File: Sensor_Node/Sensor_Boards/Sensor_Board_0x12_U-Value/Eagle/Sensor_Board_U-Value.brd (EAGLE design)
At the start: 31.5 x 57 mm, 25 parts, among them IC1 MCP3911A0-E/SS, IC2 4066D, J2 ARDUINO_ISP, U2 ATMEGA328P_TQFP, Y1 8MHZ

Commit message: Added WSN eagle library
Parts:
- moved D2 103.3 mm to (52.0, 22.0), turned to 180 degrees
- moved R1 101.1 mm to (52.0, 24.0), turned to 180 degrees
- moved Y1 94.3 mm to (50.4, 7.74)
- moved R4 84.0 mm to (47.5, 24.0)
- moved C12 83.7 mm to (43.0, 7.50)
- moved R3 78.1 mm to (47.5, 22.0), turned to 180 degrees
- moved S3 77.5 mm to (37.0, 25.5), turned to 90 degrees
- moved J2 74.6 mm to (50.0, 28.3), turned to 90 degrees
- moved C6 74.1 mm to (46.5, 7.50), turned to 180 degrees
- moved S2 57.7 mm to (38.0, 14.0), turned to 270 degrees
- moved U2 56.8 mm to (47.9, 14.6), turned to 90 degrees
- moved J1 34.2 mm to (2.34, 22.5), turned to 180 degrees
- moved D1 33.1 mm to (7.00, 17.0), turned to 0 degrees
- moved C8 29.7 mm to (7.00, 22.0), turned to 90 degrees
- moved C3 27.4 mm to (17.5, 8.50)
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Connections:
- removed net D11_MOSI: U2.15
- removed net D12_MISO: J2.P$1, J2.P$3, U2.16
- removed net D13_SCK: J2.P$2, U2.17
- removed net N$16: U2.32
- removed net N$20: U2.10
- removed net N$21: U2.11
- net ADCLK: now also U2.32
- net AD_CS: now also U2.10
- net DATA_READY: now also U2.11
- net MISO: now also J2.P$1, U2.16
- net MOSI: now also J2.P$3, U2.15
- net SCK: now also J2.P$2, U2.17
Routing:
- net DVDD: track 58.3 -> 0.00 mm
- net INPUT_EN: track 50.2 -> 0.00 mm
- net SHORT: track 48.8 -> 0.00 mm, vias 2 -> 0
- net DGND: track 43.5 -> 0.00 mm, vias 3 -> 0
- net N$8: track 25.0 -> 0.00 mm, vias 2 -> 0
- net AVDD: track 19.9 -> 0.00 mm
- net ADCLK: track 14.1 -> 0.00 mm
- net DATA_READY: track 14.1 -> 0.00 mm
- net N$12: track 12.1 -> 0.00 mm
- net N$2: track 3.74 -> 0.00 mm
- net MOSI: track 2.08 -> 0.00 mm
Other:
- board size 31.5 x 57 mm -> 55 x 35 mm

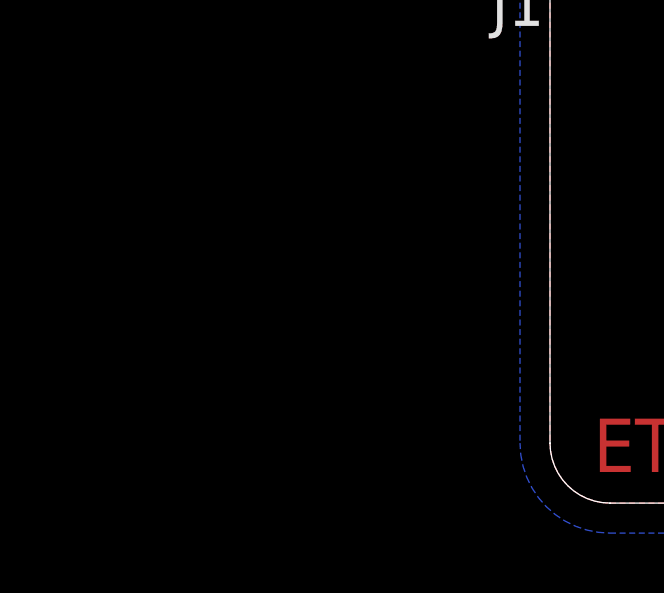
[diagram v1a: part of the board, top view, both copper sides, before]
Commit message: Update U-Value board, Added Readme for sensor boards
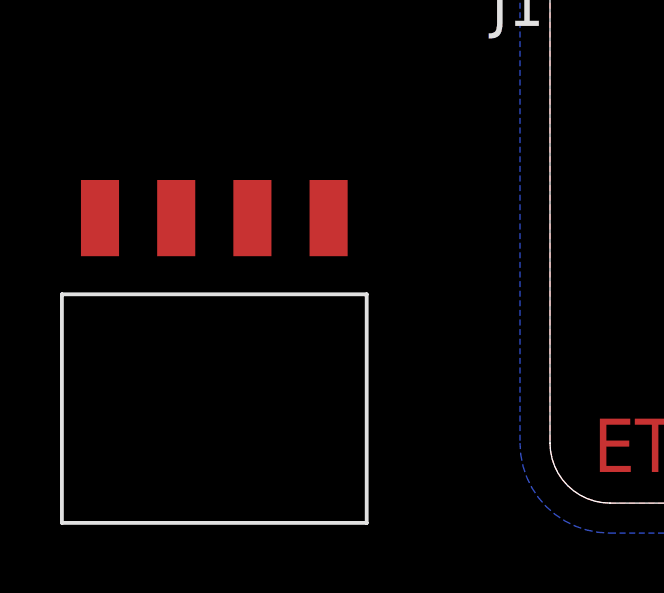
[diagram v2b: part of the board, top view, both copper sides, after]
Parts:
- added U$1: M04_SMD_90, wsn:M04_SMD_90
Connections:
- removed net N$19: U2.9
- removed net N$22: U2.12
- new net MCU_RXI: U$1.2, U2.13
- new net MCU_TXO: U$1.3, U2.12
- net GND: now also U$1.1
- net LED: now also U2.9; no longer U2.13
- net VCC: now also U$1.4
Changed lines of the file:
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@@
 </element>
 <element name="D2" library="wsn" package="LED-0603" value="" x="52" y="22" rot="R180"/>
+<element name="U$1" library="wsn" package="M04_SMD_90" value="M04_SMD_90" x="-15" y="9.5"/>
 </elements>
 <signals>
@@
 <contactref element="S2" pad="1"/>
 <contactref element="J2" pad="P$6"/>
+<contactref element="U$1" pad="4"/>
 <wire x1="49.8725" y1="18.8551" x2="48.4" y2="24" width="0" layer="19" extent="1-1"/>
 <wire x1="44.9025" y1="28.2675" x2="48.4" y2="24" width="0" layer="19" extent="1-1"/>
@@
 <wire x1="42.1" y1="7.5" x2="47.4725" y2="10.2699" width="0" layer="19" extent="1-1"/>
 <wire x1="35.3" y1="16.5" x2="42.1" y2="7.5" width="0" layer="19" extent="1-1"/>
+<wire x1="-7.38" y1="9.5" x2="35.3" y2="16.5" width="0" layer="19" extent="1-1"/>
 </signal>
 <signal name="GND">
@@
 <contactref element="Y1" pad="2"/>
 <contactref element="D2" pad="C"/>
+<contactref element="U$1" pad="1"/>
 <wire x1="37" y1="33.45" x2="44.9025" y2="30.8075" width="0" layer="19" extent="1-1"/>
 <wire x1="37" y1="25.5" x2="37" y2="33.45" width="0" layer="19" extent="1-1"/>
@@
 <wire x1="50.4" y1="7.735" x2="48.2725" y2="10.2699" width="0" layer="19" extent="1-1"/>
 <wire x1="35.3" y1="11.5" x2="43.9" y2="7.5" width="0" layer="19" extent="1-1"/>
+<wire x1="-15" y1="9.5" x2="35.3" y2="11.5" width="0" layer="19" extent="1-1"/>
 </signal>
 <signal name="N$5">
@@
 <contactref element="U2" pad="2"/>
 </signal>
-<signal name="N$19">
+<signal name="LED">
+<contactref element="R1" pad="2"/>
 <contactref element="U2" pad="9"/>
-</signal>
-<signal name="N$22">
-<contactref element="U2" pad="12"/>
-</signal>
-<signal name="LED">
-<contactref element="U2" pad="13"/>
-<contactref element="R1" pad="2"/>
-<wire x1="52.1651" y1="14.9625" x2="51.1" y2="24" width="0" layer="19" extent="1-1"/>
+<wire x1="52.1651" y1="11.7625" x2="51.1" y2="24" width="0" layer="19" extent="1-1"/>
 </signal>
 <signal name="D10_SS">
@@
 <contactref element="S2" pad="4"/>
 </signal>
+<signal name="MCU_TXO">
+<contactref element="U$1" pad="3"/>
+<contactref element="U2" pad="12"/>
+<wire x1="-9.92" y1="9.5" x2="52.1651" y2="14.1625" width="0" layer="19" extent="1-1"/>
+</signal>
+<signal name="MCU_RXI">
+<contactref element="U$1" pad="2"/>
+<contactref element="U2" pad="13"/>
+<wire x1="-12.46" y1="9.5" x2="52.1651" y2="14.9625" width="0" layer="19" extent="1-1"/>
+</signal>
 </signals>

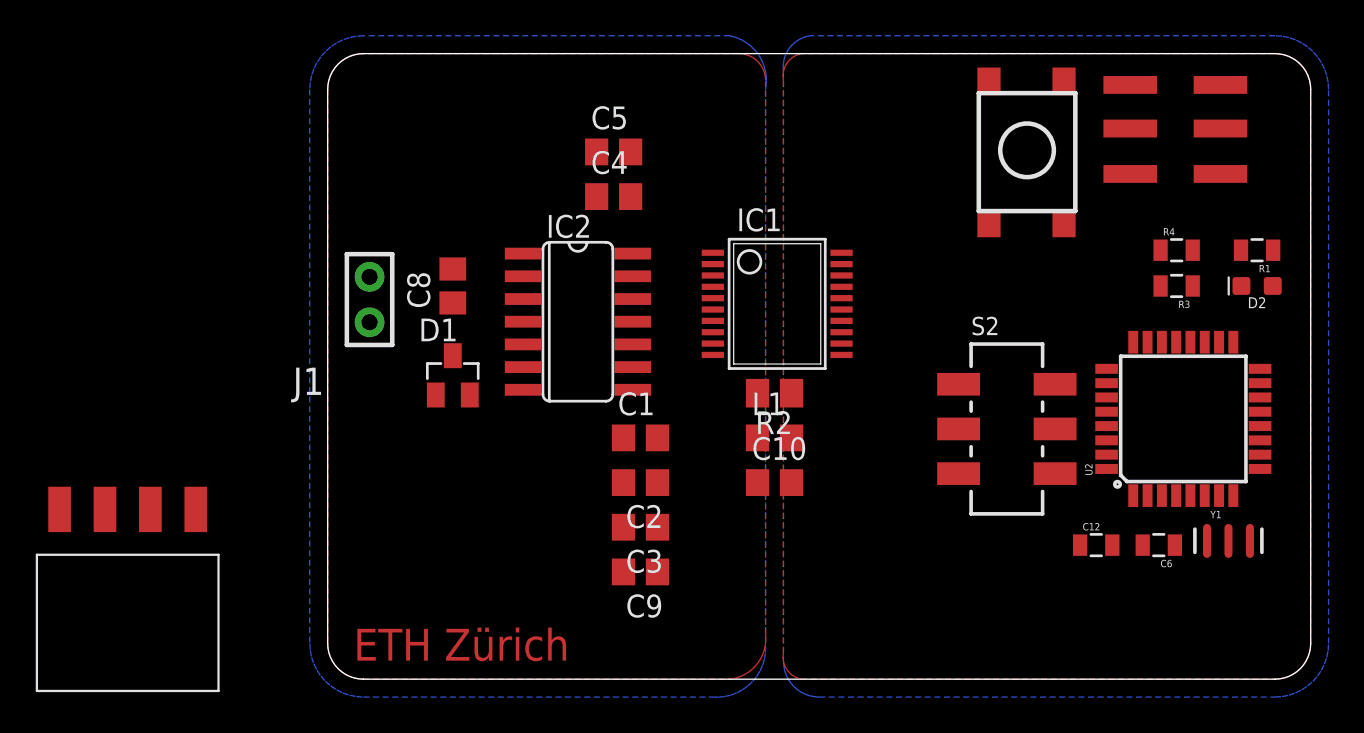
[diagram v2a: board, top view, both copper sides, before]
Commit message: Updated gatway board, updated u-value board
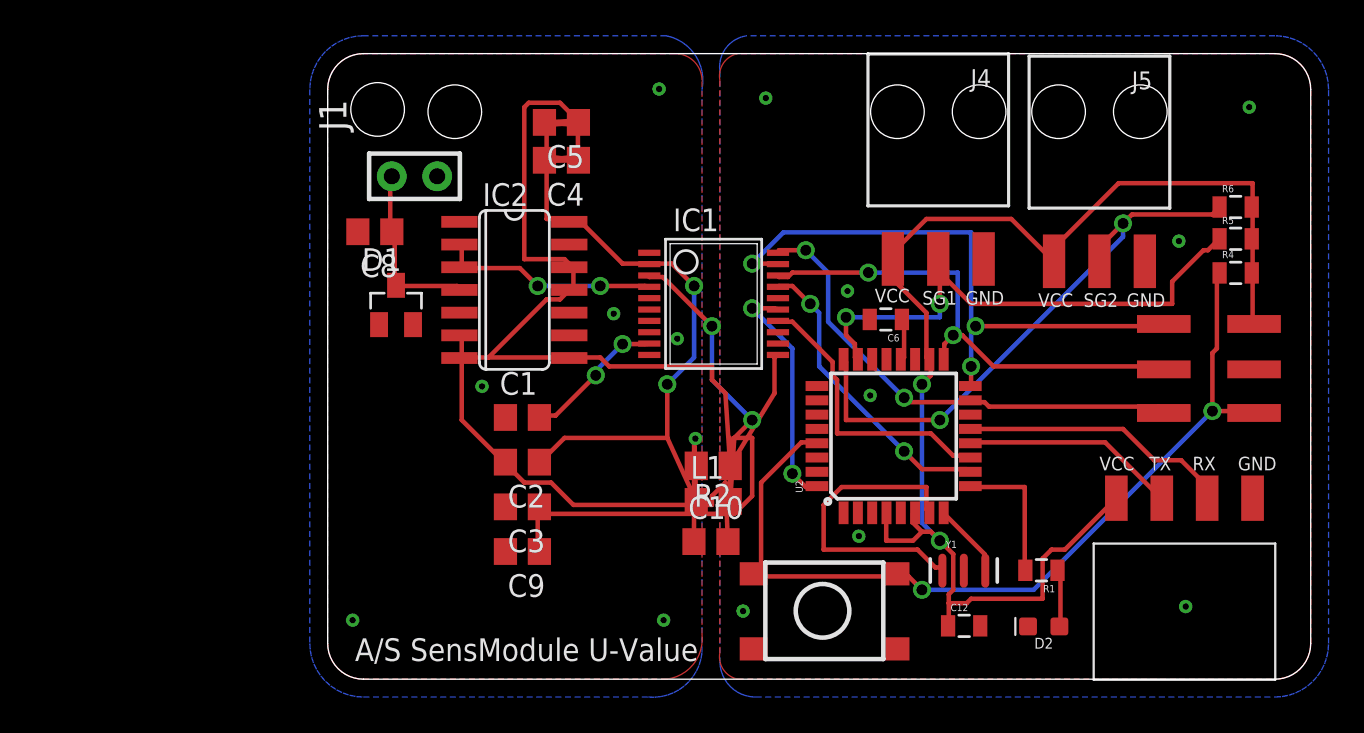
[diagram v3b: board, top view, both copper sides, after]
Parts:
- removed R3: (no value), wsn:0805
- removed S2: SLIDE_SWITCH_JS202011SCQN, wsn:JS202011SCQN
- added J4, J5: 1x3 RA Female .1", wsn:1X03_SMD_RA_FEMALE
- added R5, R6: 4.7K, wsn:0805
- moved U$1 59.1 mm to (44.1, 10.1)
- moved S3 24.4 mm to (31.8, 1.70), turned to 180 degrees
- moved D2 22.5 mm to (40.1, 2.95)
- moved R1 21.6 mm to (39.9, 6.09)
- moved C6 19.8 mm to (31.2, 20.1)
- moved U2 16.2 mm to (31.7, 13.6)
- moved Y1 14.9 mm to (35.6, 6.07)
- moved J2 8.97 mm to (46.8, 19.9), turned to 270 degrees
- moved C12 8.66 mm to (35.6, 2.98)
- moved J1 6.78 mm to (6.13, 28.1), turned to 90 degrees
- moved C1 6.70 mm to (10.9, 14.6)
- moved C2 6.70 mm to (10.9, 12.1)
- moved C3 6.70 mm to (10.9, 9.64)
- moved C9 6.70 mm to (10.9, 7.14)
- moved R2 5.32 mm to (21.6, 11.9)
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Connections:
- net N$14 renamed FTDI_TXO
- net N$15 renamed FTDI_RXI
- removed net DEBUG: R3.1
- removed net N$1: S2.6
- removed net N$26: S2.4
- removed net N$28: U2.23
- removed net N$31: R3.2, S2.2
- removed net N$5: U2.24
- new net DS18B20_1: J4.2, R5.1, U2.23
- new net DS18B20_2: J5.2, R6.1, U2.24
- new net N$15: J4.1
- net GND: now also J5.1; no longer S2.3, U$1.1
- net MCU_RXI: now also U$1.3; no longer U$1.2
- net MCU_TXO: now also U$1.2; no longer U$1.3
- net N$4: now also U$1.4; no longer S2.5
- net VCC: now also J4.3, J5.3, R5.2, R6.2, U$1.1; no longer S2.1, U$1.4
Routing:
- net DGND: track 0.00 -> 82.7 mm
- net VCC: track 0.00 -> 74.9 mm, vias 0 -> 2
- net DVDD: track 0.00 -> 50.3 mm, vias 0 -> 2
- net RESET: track 0.00 -> 50.1 mm, vias 0 -> 2
- net AVDD: track 0.00 -> 38.7 mm, vias 0 -> 2
- net MISO: track 0.00 -> 33.9 mm, vias 0 -> 3
- net DS18B20_2: track 0.00 -> 32.4 mm, vias 0 -> 2
- net DS18B20_1: track 0.00 -> 30.6 mm, vias 0 -> 2
- net SCK: track 0.00 -> 28.0 mm, vias 0 -> 2
- net MOSI: track 0.00 -> 27.2 mm, vias 0 -> 2
- net N$25: track 0.00 -> 17.3 mm
- net AD_CS: track 0.00 -> 16.8 mm, vias 0 -> 2
- net DATA_READY: track 0.00 -> 16.1 mm
- net MCU_RXI: track 0.00 -> 15.3 mm
- net ADCLK: track 0.00 -> 13.3 mm, vias 0 -> 2
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- added copper zone on layer 1, net GND
- added copper zone on layer 16, net GND
- removed copper zone on layer 1, net DGND
- removed copper zone on layer 16, net DGND
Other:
- board text added: "A/S SensModule U-Value"
- board text added: "GND"
- board text added: "RX"
- board text added: "SG1"
- board text added: "SG2"
- board text added: "TX"
- board text added: "VCC"
- board text removed: "ETH Zürich"
